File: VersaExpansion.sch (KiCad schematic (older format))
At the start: 2 parts, among them X3 PPPC202LFBN-RC, X4 PPPC202LFBN-RC

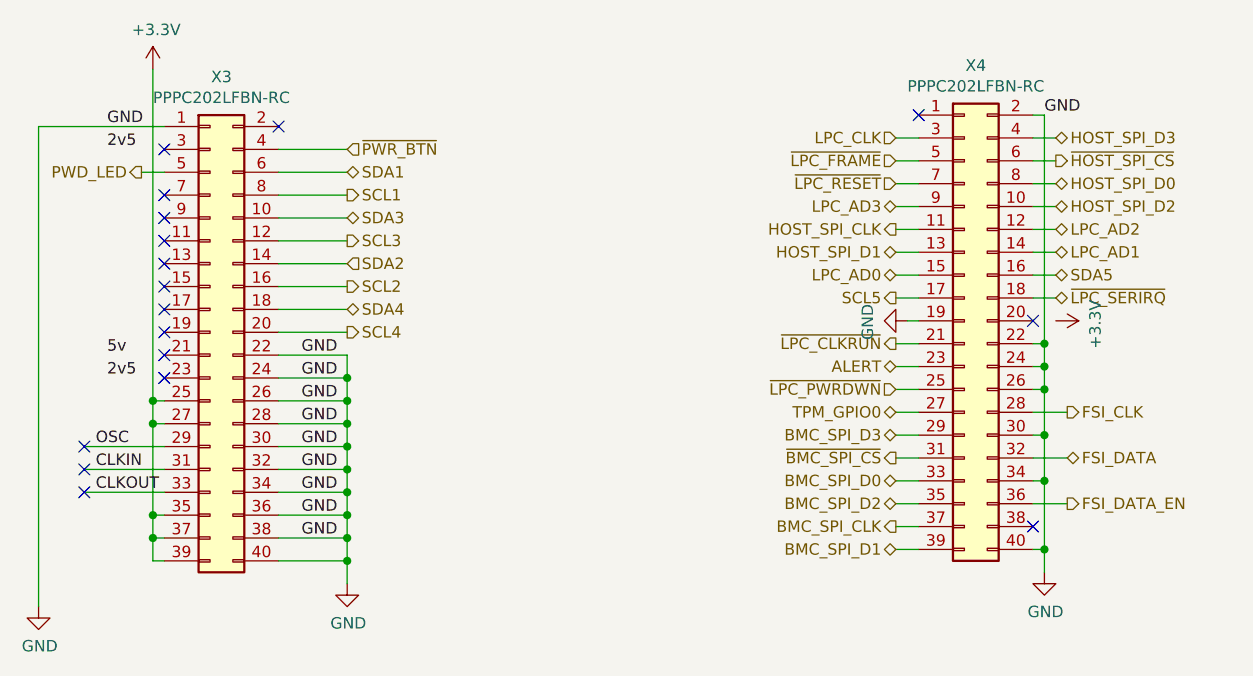
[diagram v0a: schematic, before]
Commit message: adapter: Update to version 1.1 with minor fixes found during testing.
- Fix signal naming for host/bmc SPI_CSb and SPI_CLK.
- Increase distance between FSI and TPM connector to allow for a shrowded TPM connector.
- Move R8/R9 (unused) to updated Csb signal locations.
- Fix silk screen for AVS1
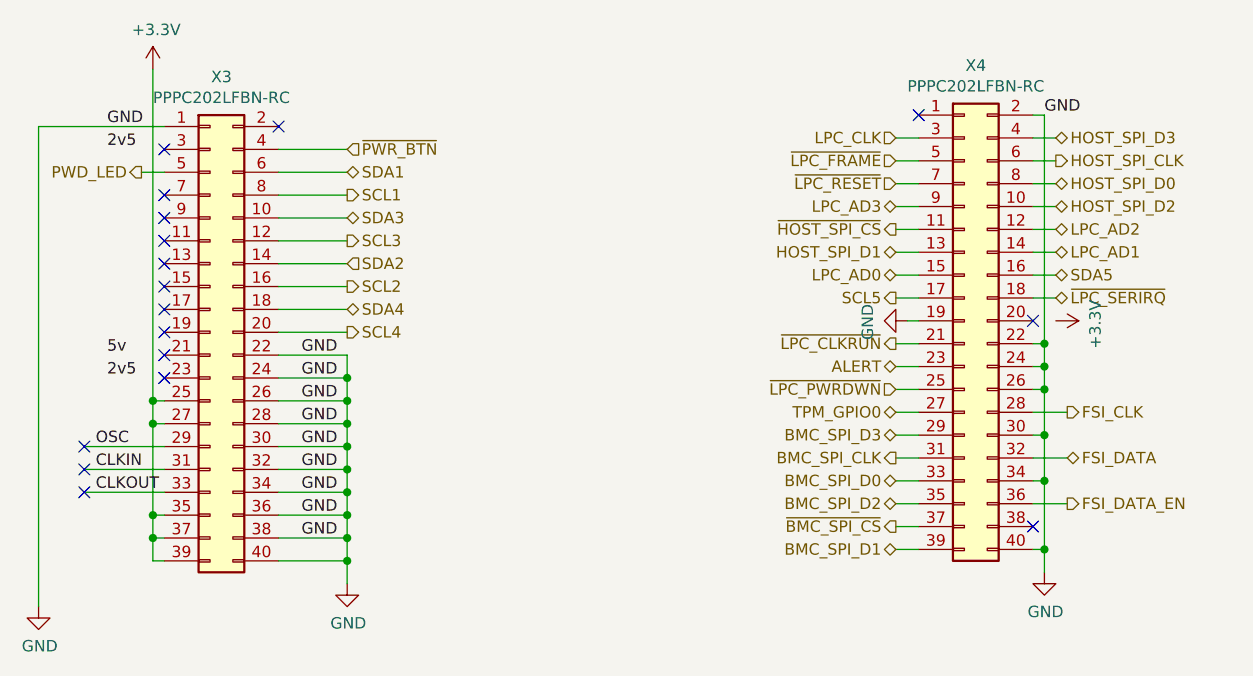
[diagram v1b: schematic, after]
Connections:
- net BMC_SPI_CLK: now also X4.31 (Pin_31); no longer X4.37 (Pin_37)
- net HOST_SPI_CLK: now also X4.6 (Pin_6); no longer X4.11 (Pin_11)
- net ~BMC_SPI_CS~: now also X4.37 (Pin_37); no longer X4.31 (Pin_31)
- net ~HOST_SPI_CS~: now also X4.11 (Pin_11); no longer X4.6 (Pin_6)
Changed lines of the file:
@@
 	5600 2000 5700 2000
 Text HLabel 5700 1700 2    50   Output ~ 0
-~HOST_SPI_CS~
+HOST_SPI_CLK
 Wire Wire Line
 	5100 1600 5000 1600
@@
 	5700 2100 5600 2100
 Text HLabel 5000 3300 0    50   Output ~ 0
-BMC_SPI_CLK
+~BMC_SPI_CS~
 Text HLabel 5000 3100 0    50   BiDi ~ 0
 BMC_SPI_D0
@@
 BMC_SPI_D1
 Text HLabel 5000 3000 0    50   Output ~ 0
-~BMC_SPI_CS~
+BMC_SPI_CLK
 Text HLabel 5000 2900 0    50   BiDi ~ 0
 BMC_SPI_D3
@@
 HOST_SPI_D1
 Text HLabel 5000 2000 0    50   Output ~ 0
-HOST_SPI_CLK
+~HOST_SPI_CS~
 Text HLabel 5000 3200 0    50   BiDi ~ 0
 BMC_SPI_D2

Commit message: v1.1: Connect LPC_CLK to A12 (was PWR_LED), add pull resistor for SERIRQ.
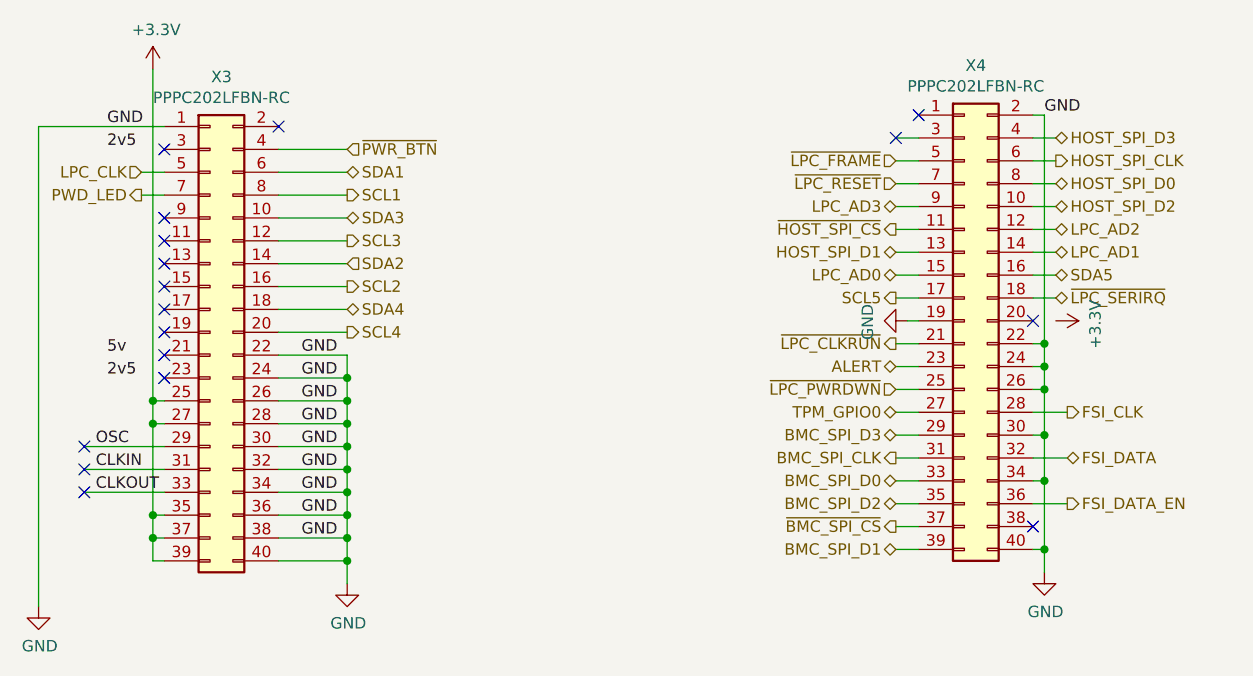
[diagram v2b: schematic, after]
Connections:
- net LPC_CLK: now also X3.5 (Pin_5); no longer X4.3 (Pin_3)
- net PWD_LED: now also X3.7 (Pin_7); no longer X3.5 (Pin_5)
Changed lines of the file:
@@
 NoConn ~ 1800 2650
 NoConn ~ 1450 3150
-NoConn ~ 1450 3050
 NoConn ~ 1450 2950
 Wire Wire Line
@@
 	1450 3150 1800 3150
 Wire Wire Line
-	1450 3050 1800 3050
-Wire Wire Line
 	1450 2950 1800 2950
 Wire Wire Line
@@
 Text HLabel 5700 1800 2    50   BiDi ~ 0
 HOST_SPI_D0
-Text HLabel 5000 1600 0    50   Input ~ 0
+Text HLabel 1700 1750 0    50   Input ~ 0
 LPC_CLK
 Wire Wire Line
@@
 Text HLabel 2600 1650 2    50   Input ~ 0
 ~PWR_BTN~
-Text HLabel 1700 1750 0    50   Output ~ 0
+Text HLabel 1700 1850 0    50   Output ~ 0
 PWD_LED
 Wire Wire Line
 	2300 1650 2600 1650
 Wire Wire Line
-	1700 1750 1800 1750
-$Comp
-L Connector_Generic:Conn_02x20_Odd_Even X?
-U 1 1 60315130
-P 5300 2400
-AR Path="/60315130" Ref="X?"  Part="1"
-AR Path="/602D8BC4/60315130" Ref="X4"  Part="1"
-F 0 "X4" H 5350 3517 50  0000 C CNN
-F 1 "PPPC202LFBN-RC" H 5350 3426 50  0000 C CNN
-F 2 "Connector_PinHeader_2.54mm:PinHeader_2x20_P2.54mm_Vertical" H 5300 2400 50  0001 C CNN
-F 3 "~" H 5300 2400 50  0001 C CNN
-	1    5300 2400
-	1    0    0    -1
-$EndComp
+	1700 1850 1800 1850
 NoConn ~ 5600 2400
 $Comp
@@
 $EndComp
 NoConn ~ 1800 1650
-NoConn ~ 1800 1850
 NoConn ~ 1800 1950
 NoConn ~ 1800 2050
@@
 NoConn ~ 1800 2350
 NoConn ~ 1800 2450
+$Comp
+L Connector_Generic:Conn_02x20_Odd_Even X?
+U 1 1 60315130
+P 5300 2400
+AR Path="/60315130" Ref="X?"  Part="1"
+AR Path="/602D8BC4/60315130" Ref="X4"  Part="1"
+F 0 "X4" H 5350 3517 50  0000 C CNN
+F 1 "PPPC202LFBN-RC" H 5350 3426 50  0000 C CNN
+F 2 "Connector_PinHeader_2.54mm:PinHeader_2x20_P2.54mm_Vertical" H 5300 2400 50  0001 C CNN
+F 3 "~" H 5300 2400 50  0001 C CNN
+	1    5300 2400
+	1    0    0    -1
+$EndComp
+NoConn ~ 5000 1600
+Wire Wire Line
+	1800 1750 1700 1750
+NoConn ~ 1450 3050
+Wire Wire Line
+	1450 3050 1800 3050
 $EndSCHEMATC
